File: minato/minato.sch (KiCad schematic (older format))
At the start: 234 parts, among them J1 Conn_ARM_JTAG_SWD_10, J2 USB_C_Receptacle_USB2.0, Q1 DTC123J, SW1 SW_Push, U1 MCP1700-3302E_SOT23, U2 STM32F103C8Tx, Y1 16MHz

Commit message: :construction: More PCB work
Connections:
- net Col0: now also D1.2 (A), D10.2 (A), D11.2 (A), D17.2 (A), D2.2 (A), D3.2 (A), D4.2 (A), D5.2 (A), D6.2 (A), D7.2 (A), D8.2 (A), D9.2 (A); no longer MX0:0.1 (COL), MX0:1.1 (COL), MX0:10.1 (COL), MX0:2.1 (COL), MX0:3.1 (COL), MX0:4.1 (COL), MX0:5.1 (COL), MX0:6.1 (COL), MX0:7.1 (COL), MX0:8.1 (COL), MX0:9.1 (COL)
- net Col1: now also D12.2 (A), D13.2 (A), D14.2 (A), D15.2 (A), D16.2 (A), D18.2 (A), D19.2 (A), D20.2 (A), D21.2 (A), D25.2 (A), D27.2 (A), D30.2 (A); no longer MX1:0.1 (COL), MX1:1.1 (COL), MX1:11.1 (COL), MX1:2.1 (COL), MX1:3.1 (COL), MX1:4.1 (COL), MX1:5.1 (COL), MX1:6.1 (COL), MX1:8.1 (COL), MX1:9.1 (COL)
- net Col2: now also D22.2 (A), D23.2 (A), D24.2 (A), D26.2 (A), D28.2 (A), D29.2 (A), D33.2 (A), D34.2 (A), D35.2 (A), D36.2 (A), D40.2 (A), D42.2 (A); no longer MX2:0.1 (COL), MX2:1.1 (COL), MX2:10.1 (COL), MX2:11.1 (COL), MX2:2.1 (COL), MX2:3.1 (COL), MX2:4.1 (COL), MX2:6.1 (COL), MX2:8.1 (COL)
- net Col3: now also D31.2 (A), D32.2 (A), D37.2 (A), D38.2 (A), D39.2 (A), D41.2 (A), D45.2 (A), D46.2 (A), D47.2 (A), D51.2 (A), D78.2 (A), D84.2 (A); no longer MX3:0.1 (COL), MX3:1.1 (COL), MX3:10.1 (COL), MX3:11.1 (COL), MX3:2.1 (COL), MX3:3.1 (COL), MX3:4.1 (COL), MX3:5.1 (COL), MX3:6.1 (COL), MX3:7.1 (COL), MX3:8.1 (COL), MX3:9.1 (COL)
- net Col4: now also D43.2 (A), D44.2 (A), D48.2 (A), D49.2 (A), D50.2 (A), D52.2 (A), D55.2 (A), D56.2 (A), D57.2 (A), D61.2 (A), D90.2 (A), D95.2 (A); no longer MX4:0.1 (COL), MX4:1.1 (COL), MX4:2.1 (COL), MX4:3.1 (COL), MX4:4.1 (COL), MX4:5.1 (COL), MX4:6.1 (COL), MX4:7.1 (COL), MX4:8.1 (COL), MX4:9.1 (COL)
- net Col5: now also D105.2 (A), D53.2 (A), D54.2 (A), D58.2 (A), D59.2 (A), D60.2 (A), D62.2 (A), D65.2 (A), D66.2 (A), D67.2 (A), D71.2 (A), D99.2 (A); no longer MX5:0.1 (COL), MX5:1.1 (COL), MX5:2.1 (COL), MX5:3.1 (COL), MX5:4.1 (COL), MX5:5.1 (COL), MX5:6.1 (COL), MX5:7.1 (COL), MX5:8.1 (COL), MX5:9.1 (COL)
- net Col6: now also D63.2 (A), D64.2 (A), D68.2 (A), D69.2 (A), D70.2 (A), D72.2 (A), D75.2 (A), D76.2 (A), D77.2 (A), D82.2 (A); no longer MX6:0.1 (COL), MX6:1.1 (COL), MX6:2.1 (COL), MX6:3.1 (COL), MX6:4.1 (COL), MX6:5.1 (COL), MX6:6.1 (COL), MX6:7.1 (COL), MX6:8.1 (COL), MX6:9.1 (COL)
- net Col7: now also D73.2 (A), D74.2 (A), D79.2 (A), D80.2 (A), D81.2 (A), D83.2 (A), D87.2 (A), D88.2 (A), D89.2 (A), D94.2 (A); no longer MX7:0.1 (COL), MX7:1.1 (COL), MX7:10.1 (COL), MX7:11.1 (COL), MX7:2.1 (COL), MX7:3.1 (COL), MX7:4.1 (COL), MX7:5.1 (COL), MX7:6.1 (COL), MX7:7.1 (COL), MX7:8.1 (COL), MX7:9.1 (COL)
- net Col8: now also D103.2 (A), D104.2 (A), D85.2 (A), D86.2 (A), D91.2 (A), D92.2 (A), D93.2 (A), D97.2 (A), D98.2 (A); no longer MX8:0.1 (COL), MX8:1.1 (COL), MX8:10.1 (COL), MX8:11.1 (COL), MX8:2.1 (COL), MX8:3.1 (COL), MX8:4.1 (COL), MX8:5.1 (COL), MX8:6.1 (COL), MX8:7.1 (COL), MX8:9.1 (COL)
- net Col9: now also D100.2 (A), D101.2 (A), D102.2 (A), D96.2 (A); no longer MX9:0.1 (COL), MX9:1.1 (COL), MX9:10.1 (COL), MX9:11.1 (COL), MX9:2.1 (COL), MX9:4.1 (COL), MX9:5.1 (COL), MX9:6.1 (COL), MX9:8.1 (COL), MX9:9.1 (COL)
- net Row0: now also MX0:0.2 (ROW), MX1:0.2 (ROW), MX2:0.2 (ROW), MX3:0.2 (ROW), MX4:0.2 (ROW), MX5:0.2 (ROW), MX6:0.2 (ROW), MX7:0.2 (ROW), MX8:0.2 (ROW), MX9:0.2 (ROW); no longer D1.1 (K), D12.1 (K), D22.1 (K), D31.1 (K), D43.1 (K), D53.1 (K), D63.1 (K), D73.1 (K), D85.1 (K), D96.1 (K)
- net Row1: now also MX0:1.2 (ROW), MX1:1.2 (ROW), MX2:1.2 (ROW), MX3:1.2 (ROW), MX4:1.2 (ROW), MX5:1.2 (ROW), MX6:1.2 (ROW), MX7:1.2 (ROW), MX8:1.2 (ROW), MX9:1.2 (ROW); no longer D100.1 (K), D18.1 (K), D28.1 (K), D37.1 (K), D48.1 (K), D58.1 (K), D68.1 (K), D7.1 (K), D79.1 (K), D91.1 (K)
- net Row10: now also MX0:10.2 (ROW), MX2:10.2 (ROW), MX3:10.2 (ROW), MX7:10.2 (ROW), MX8:10.2 (ROW), MX9:10.2 (ROW); no longer D27.1 (K), D36.1 (K), D6.1 (K), D78.1 (K), D90.1 (K), D99.1 (K)
- net Row11: now also MX1:11.2 (ROW), MX2:11.2 (ROW), MX3:11.2 (ROW), MX7:11.2 (ROW), MX8:11.2 (ROW), MX9:11.2 (ROW); no longer D105.1 (K), D17.1 (K), D30.1 (K), D42.1 (K), D84.1 (K), D95.1 (K)
- net Row2: now also MX0:2.2 (ROW), MX1:2.2 (ROW), MX2:2.2 (ROW), MX3:2.2 (ROW), MX4:2.2 (ROW), MX5:2.2 (ROW), MX6:2.2 (ROW), MX7:2.2 (ROW), MX8:2.2 (ROW), MX9:2.2 (ROW); no longer D101.1 (K), D13.1 (K), D2.1 (K), D23.1 (K), D32.1 (K), D44.1 (K), D54.1 (K), D64.1 (K), D74.1 (K), D86.1 (K)
- net Row3: now also MX0:3.2 (ROW), MX1:3.2 (ROW), MX2:3.2 (ROW), MX3:3.2 (ROW), MX4:3.2 (ROW), MX5:3.2 (ROW), MX6:3.2 (ROW), MX7:3.2 (ROW), MX8:3.2 (ROW); no longer D19.1 (K), D29.1 (K), D38.1 (K), D49.1 (K), D59.1 (K), D69.1 (K), D8.1 (K), D80.1 (K), D92.1 (K)
- net Row4: now also MX0:4.2 (ROW), MX1:4.2 (ROW), MX2:4.2 (ROW), MX3:4.2 (ROW), MX4:4.2 (ROW), MX5:4.2 (ROW), MX6:4.2 (ROW), MX7:4.2 (ROW), MX8:4.2 (ROW), MX9:4.2 (ROW); no longer D102.1 (K), D14.1 (K), D24.1 (K), D3.1 (K), D39.1 (K), D50.1 (K), D60.1 (K), D70.1 (K), D81.1 (K), D93.1 (K)
- net Row5: now also MX0:5.2 (ROW), MX1:5.2 (ROW), MX3:5.2 (ROW), MX4:5.2 (ROW), MX5:5.2 (ROW), MX6:5.2 (ROW), MX7:5.2 (ROW), MX8:5.2 (ROW), MX9:5.2 (ROW); no longer D20.1 (K), D33.1 (K), D45.1 (K), D55.1 (K), D65.1 (K), D75.1 (K), D87.1 (K), D9.1 (K), D97.1 (K)
- net Row6: now also MX0:6.2 (ROW), MX1:6.2 (ROW), MX3:6.2 (ROW), MX4:6.2 (ROW), MX5:6.2 (ROW), MX6:6.2 (ROW), MX7:6.2 (ROW), MX8:6.2 (ROW), MX9:6.2 (ROW); no longer D103.1 (K), D15.1 (K), D34.1 (K), D4.1 (K), D46.1 (K), D56.1 (K), D66.1 (K), D76.1 (K), D88.1 (K)
- net Row7: now also MX0:7.2 (ROW), MX2:6.2 (ROW), MX3:7.2 (ROW), MX4:7.2 (ROW), MX5:7.2 (ROW), MX6:7.2 (ROW), MX7:7.2 (ROW), MX8:7.2 (ROW); no longer D10.1 (K), D25.1 (K), D40.1 (K), D51.1 (K), D61.1 (K), D71.1 (K), D82.1 (K), D94.1 (K)
- net Row8: now also MX0:8.2 (ROW), MX1:8.2 (ROW), MX2:8.2 (ROW), MX3:8.2 (ROW), MX4:8.2 (ROW), MX5:8.2 (ROW), MX6:8.2 (ROW), MX7:8.2 (ROW), MX9:8.2 (ROW); no longer D16.1 (K), D26.1 (K), D41.1 (K), D5.1 (K), D52.1 (K), D62.1 (K), D72.1 (K), D83.1 (K), D98.1 (K)
- net Row9: now also MX0:9.2 (ROW), MX1:9.2 (ROW), MX3:9.2 (ROW), MX4:9.2 (ROW), MX5:9.2 (ROW), MX6:9.2 (ROW), MX7:9.2 (ROW), MX8:9.2 (ROW), MX9:9.2 (ROW); no longer D104.1 (K), D11.1 (K), D21.1 (K), D35.1 (K), D47.1 (K), D57.1 (K), D67.1 (K), D77.1 (K), D89.1 (K)
- new net: D1.1 (K), MX0:0.1 (COL)
- new net: D7.1 (K), MX0:1.1 (COL)
- new net: D12.1 (K), MX1:0.1 (COL)
- new net: D18.1 (K), MX1:1.1 (COL)
- new net: D2.1 (K), MX0:2.1 (COL)
- new net: D8.1 (K), MX0:3.1 (COL)
- new net: D13.1 (K), MX1:2.1 (COL)
- new net: D19.1 (K), MX1:3.1 (COL)
- new net: D3.1 (K), MX0:4.1 (COL)
- new net: D9.1 (K), MX0:5.1 (COL)
- new net: D14.1 (K), MX1:4.1 (COL)
- new net: D4.1 (K), MX0:6.1 (COL)
- new net: D10.1 (K), MX0:7.1 (COL)
- new net: D15.1 (K), MX1:6.1 (COL)
- new net: D20.1 (K), MX1:5.1 (COL)
- new net: D5.1 (K), MX0:8.1 (COL)
- new net: D11.1 (K), MX0:9.1 (COL)
- new net: D16.1 (K), MX1:8.1 (COL)
- new net: D21.1 (K), MX1:9.1 (COL)
- new net: D6.1 (K), MX0:10.1 (COL)
- new net: D17.1 (K), MX1:11.1 (COL)
- new net: D22.1 (K), MX2:0.1 (COL)
- new net: D23.1 (K), MX2:2.1 (COL)
- new net: D24.1 (K), MX2:4.1 (COL)
- new net: D25.1 (K), MX2:6.1 (COL)
- new net: D26.1 (K), MX2:8.1 (COL)
- new net: D27.1 (K), MX2:10.1 (COL)
- new net: D28.1 (K), MX2:1.1 (COL)
- new net: D29.1 (K), MX2:3.1 (COL)
- new net: D30.1 (K), MX2:11.1 (COL)
- new net: D31.1 (K), MX3:0.1 (COL)
- new net: D32.1 (K), MX3:2.1 (COL)
- new net: D33.1 (K), MX3:5.1 (COL)
- new net: D34.1 (K), MX3:6.1 (COL)
- new net: D35.1 (K), MX3:9.1 (COL)
- new net: D36.1 (K), MX3:10.1 (COL)
- new net: D37.1 (K), MX3:1.1 (COL)
- new net: D38.1 (K), MX3:3.1 (COL)
- new net: D39.1 (K), MX3:4.1 (COL)
- new net: D40.1 (K), MX3:7.1 (COL)
- new net: D41.1 (K), MX3:8.1 (COL)
- new net: D42.1 (K), MX3:11.1 (COL)
- new net: D43.1 (K), MX4:0.1 (COL)
- new net: D44.1 (K), MX4:2.1 (COL)
- new net: D45.1 (K), MX4:5.1 (COL)
- new net: D46.1 (K), MX4:6.1 (COL)
- new net: D47.1 (K), MX4:9.1 (COL)
- new net: D48.1 (K), MX4:1.1 (COL)
- new net: D49.1 (K), MX4:3.1 (COL)
- new net: D50.1 (K), MX4:4.1 (COL)
- new net: D51.1 (K), MX4:7.1 (COL)
- new net: D52.1 (K), MX4:8.1 (COL)
- new net: D53.1 (K), MX5:0.1 (COL)
- new net: D54.1 (K), MX5:2.1 (COL)
- new net: D55.1 (K), MX5:5.1 (COL)
- new net: D56.1 (K), MX5:6.1 (COL)
- new net: D57.1 (K), MX5:9.1 (COL)
- new net: D58.1 (K), MX5:1.1 (COL)
- new net: D59.1 (K), MX5:3.1 (COL)
- new net: D60.1 (K), MX5:4.1 (COL)
- new net: D61.1 (K), MX5:7.1 (COL)
- new net: D62.1 (K), MX5:8.1 (COL)
- new net: D63.1 (K), MX6:0.1 (COL)
- new net: D64.1 (K), MX6:2.1 (COL)
- new net: D65.1 (K), MX6:5.1 (COL)
- new net: D66.1 (K), MX6:6.1 (COL)
- new net: D67.1 (K), MX6:9.1 (COL)
- new net: D68.1 (K), MX6:1.1 (COL)
- new net: D69.1 (K), MX6:3.1 (COL)
- new net: D70.1 (K), MX6:4.1 (COL)
- new net: D71.1 (K), MX6:7.1 (COL)
- new net: D72.1 (K), MX6:8.1 (COL)
- new net: D73.1 (K), MX7:0.1 (COL)
- new net: D74.1 (K), MX7:2.1 (COL)
- new net: D75.1 (K), MX7:5.1 (COL)
- new net: D76.1 (K), MX7:6.1 (COL)
- new net: D77.1 (K), MX7:9.1 (COL)
- new net: D78.1 (K), MX7:10.1 (COL)
- new net: D79.1 (K), MX7:1.1 (COL)
- new net: D80.1 (K), MX7:3.1 (COL)
- new net: D81.1 (K), MX7:4.1 (COL)
- new net: D82.1 (K), MX7:7.1 (COL)
- new net: D83.1 (K), MX7:8.1 (COL)
- new net: D84.1 (K), MX7:11.1 (COL)
- new net: D85.1 (K), MX8:0.1 (COL)
- new net: D86.1 (K), MX8:2.1 (COL)
- new net: D87.1 (K), MX8:5.1 (COL)
- new net: D88.1 (K), MX8:6.1 (COL)
- new net: D89.1 (K), MX8:9.1 (COL)
- new net: D90.1 (K), MX8:10.1 (COL)
- new net: D91.1 (K), MX8:1.1 (COL)
- new net: D92.1 (K), MX8:3.1 (COL)
- new net: D93.1 (K), MX8:4.1 (COL)
- new net: D94.1 (K), MX8:7.1 (COL)
- new net: D95.1 (K), MX8:11.1 (COL)
- new net: D96.1 (K), MX9:0.1 (COL)
- new net: D97.1 (K), MX9:5.1 (COL)
- new net: D98.1 (K), MX9:8.1 (COL)
- new net: D99.1 (K), MX9:10.1 (COL)
- new net: D100.1 (K), MX9:1.1 (COL)
- new net: D101.1 (K), MX9:2.1 (COL)
- new net: D102.1 (K), MX9:4.1 (COL)
- new net: D103.1 (K), MX9:6.1 (COL)
- new net: D104.1 (K), MX9:9.1 (COL)
- new net: D105.1 (K), MX9:11.1 (COL)
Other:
- moved on the sheet: D1, D10, D100, D101, D102, D103, D104, D105, D11, D12, D13, D14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

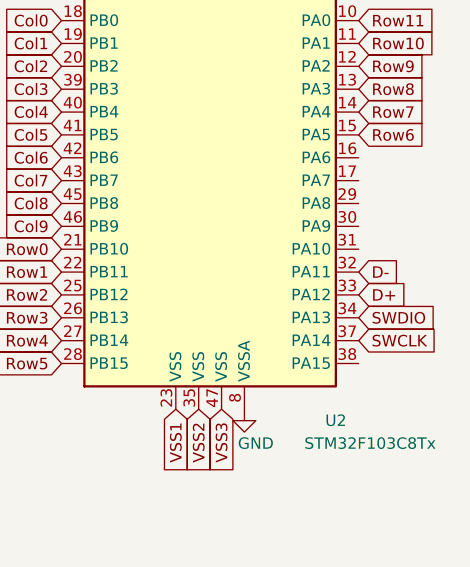
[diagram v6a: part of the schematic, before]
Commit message: :sparkles: Place components on PCB
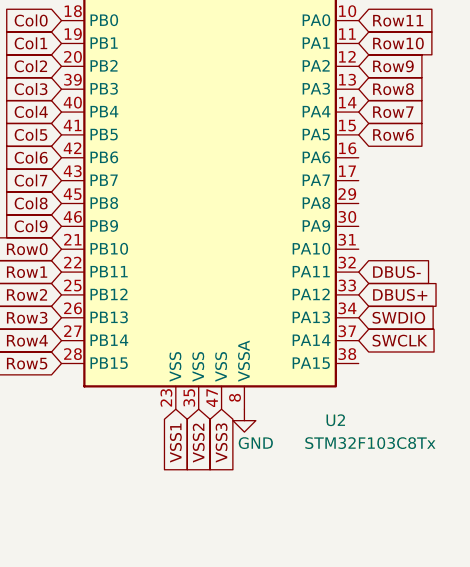
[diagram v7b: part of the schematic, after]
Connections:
- net D+ is gone; now on net DBUS+: U2.33 (PA12)
- net D- is gone; now on net DBUS-: U2.32 (PA11)
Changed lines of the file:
@@
 SWDIO
 Text GLabel 14750 3950 2    50   Input ~ 0
-D-
+DBUS-
 Text GLabel 14750 4050 2    50   Input ~ 0
-D+
+DBUS+
 Text GLabel 13450 1750 0    50   Input ~ 0
 NRST
